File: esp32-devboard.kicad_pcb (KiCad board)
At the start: 4 copper layers, 38 parts, among them J1 USB_C_Receptacle_USB2.0_16P, J2 CA, J3 CB, SW1 BOOT, SW2 RST, SW3 FLIP, SW4 FLOP, U1 ESP32-C6-MINI-1/U, U2 AMS1117-3.3

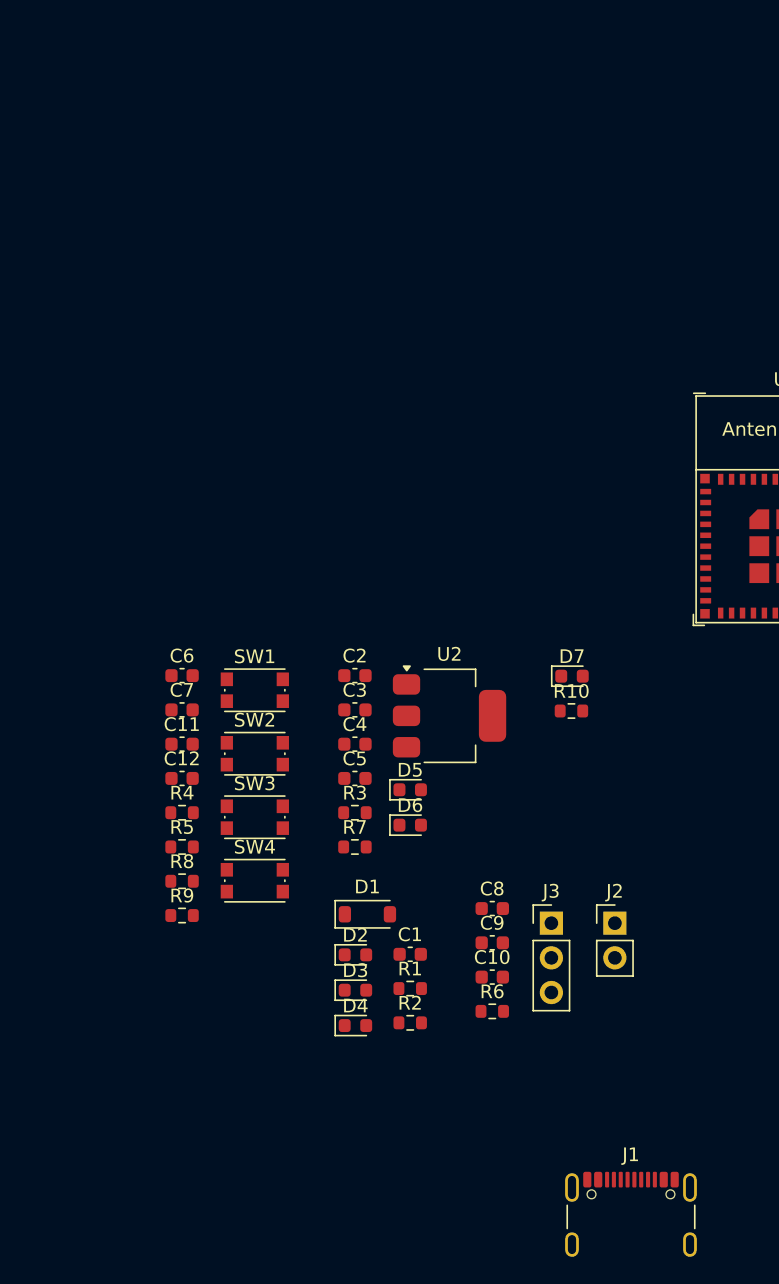
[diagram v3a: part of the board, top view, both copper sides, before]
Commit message: LDO layout>
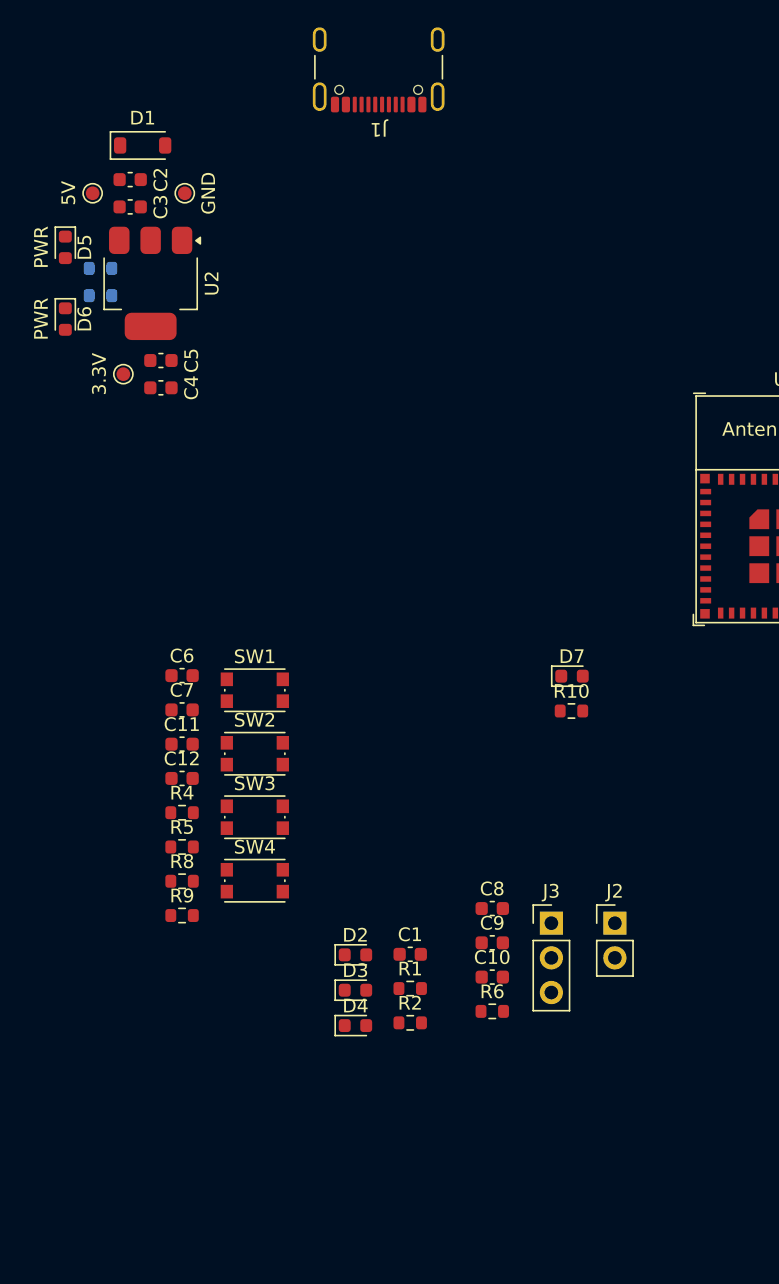
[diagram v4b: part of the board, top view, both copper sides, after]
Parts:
- added TP1: 5V, TestPoint:TestPoint_Pad_D1.0mm, F.Cu at (93.2, 68.0)
- added TP2: 3.3V, TestPoint:TestPoint_Pad_D1.0mm, F.Cu at (95.5, 81.2)
- added TP3: GND, TestPoint:TestPoint_Pad_D1.0mm, F.Cu at (100.0, 68.0)
- R3, R7: moved to B.Cu
- moved J1 88.1 mm to (114.2, 57.8), turned to 180 degrees
- moved D1 58.7 mm to (96.9, 64.5)
- moved D5 47.1 mm to (91.2, 72.0), turned to -90 degrees
- moved D6 44.9 mm to (91.2, 77.2), turned to -90 degrees
- moved R7 44.5 mm to (93.8, 75.5), turned to 180 degrees
- moved R3 44.0 mm to (93.8, 73.5), turned to 180 degrees
- moved C3 40.3 mm to (96.0, 69.0)
- moved C2 39.9 mm to (96.0, 67.0)
- moved U2 38.5 mm to (97.5, 74.6), turned to -90 degrees
- moved C5 33.7 mm to (98.2, 80.2)
- moved C4 29.7 mm to (98.2, 82.2)

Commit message: more pwr stuff
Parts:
- moved TP3 0.25 mm to (100.2, 68.0)
- moved C2 0.22 mm to (96.2, 67.0)
- moved C3 0.22 mm to (96.2, 69.0)
- moved D1 0.08 mm to (97.0, 64.5)
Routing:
- added copper zone on F.Cu, net +3.3V
- added copper zone on F.Cu, net /Power/+5V
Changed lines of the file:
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@@
 	(footprint "TestPoint:TestPoint_Pad_D1.0mm"
 		(layer "F.Cu")
-		(at 100 68 -90)
+		(at 100.25 68 -90)
 		(descr "SMD pad as test Point, diameter 1.0mm")
 		(tags "test point SMD pad")
@@
 	(footprint "Diode_SMD:D_SOD-123"
 		(layer "F.Cu")
-		(at 96.915 64.5)
+		(at 97 64.5)
 		(descr "SOD-123")
 		(tags "SOD-123")
@@
 	(footprint "Capacitor_SMD:C_0603_1608Metric"
 		(layer "F.Cu")
-		(at 96 67)
+		(at 96.225 67)
 		(descr "Capacitor SMD 0603 (1608 Metric), square (rectangular) end terminal, IPC_7351 nominal, (Body size source: IPC-SM-782 page 76, https://www.pcb-3d.com/wordpress/wp-content/uploads/ipc-sm-782a_amendment_1_and_2.pdf), generated with kicad-footprint-generator")
 		(tags "capacitor")
@@
 	(footprint "Capacitor_SMD:C_0603_1608Metric"
 		(layer "F.Cu")
-		(at 96 69)
+		(at 96.225 69)
 		(descr "Capacitor SMD 0603 (1608 Metric), square (rectangular) end terminal, IPC_7351 nominal, (Body size source: IPC-SM-782 page 76, https://www.pcb-3d.com/wordpress/wp-content/uploads/ipc-sm-782a_amendment_1_and_2.pdf), generated with kicad-footprint-generator")
 		(tags "capacitor")
@@
 	)
 	(zone
+		(net 29)
+		(net_name "+3.3V")
+		(layer "F.Cu")
+		(hatch edge 0.5)
+		(priority 1)
+		(connect_pads yes
+			(clearance 0)
+		)
+		(min_thickness 0.25)
+		(filled_areas_thickness no)
+		(fill yes
+			(thermal_gap 0.5)
+			(thermal_bridge_width 0.5)
+		)
+		(polygon
+			(pts
+				(xy 98.25 82.75) (xy 96.75 82.75) (xy 96 82) (xy 94.75 82) (xy 94.75 80.25) (xy 95.5 79.5) (xy 95.5 78.25)
+				(xy 95.5 78.25) (xy 98.25 78.25)
+			)
+		)
+	)
+	(zone
+		(net 38)
+		(net_name "/Power/+5V")
+		(layer "F.Cu")
+		(hatch edge 0.5)
+		(priority 2)
+		(connect_pads yes
+			(clearance 0)
+		)
+		(min_thickness 0.25)
+		(filled_areas_thickness no)
+		(fill yes
+			(thermal_gap 0.5)
+			(thermal_bridge_width 0.5)
+		)
+		(polygon
+			(pts
+				(xy 96.25 72.75) (xy 94.25 72.75) (xy 94.25 70.25) (xy 93.5 69.5) (xy 92.25 69.5) (xy 92.25 66.5)
+				(xy 93.75 66.5) (xy 94.5 65.75) (xy 94.5 63.25) (xy 96.25 63.25)
+			)
+		)
+	)
+	(zone
+		(net 29)
+		(net_name "+3.3V")
+		(layer "F.Cu")
+		(hatch edge 0.5)
+		(connect_pads yes
+			(clearance 0)
+		)
+		(min_thickness 0.25)
+		(filled_areas_thickness no)
+		(fill yes
+			(thermal_gap 0.5)
+			(thermal_bridge_width 0.5)
+		)
+		(polygon
+			(pts
+				(xy 95.5 79) (xy 95.5 76.5) (xy 95.5 76.5) (xy 96.5 75.5) (xy 96.5 70.25) (xy 98.5 70.25) (xy 98.5 75.5)
+				(xy 99.5 76.5) (xy 99.5 76.5) (xy 99.5 79)
+			)
+		)
+	)
+	(zone
 		(net 0)
 		(net_name "")
@@
 		(members "9e491c97-c408-47aa-a825-656574b5255b" "efe0206d-e05d-4263-8e52-4d6ee51e22c0")
 	)
-	(group ""
-		(members "1b6c8068-067f-474c-ba5a-769a4012d6b8" "262f769d-a23a-4fdd-95f2-37f04a277f88"
-			"486c2cc9-136b-4f64-8c2a-f94eec6c1d56" "4a1526ff-0a48-487e-8273-066df841240d"
-			"54078b00-5d86-4ed3-92e5-de67855fb4d0" "5a667fe3-618f-45d0-b3d5-f59ddde55a9a"
-			"7ea36561-44c1-4dda-9039-b84add404954" "9e30236c-4aae-4ac8-98ee-09181bec6437"
-			"a3e8463d-94b6-462c-b727-42dbfcba4cf4" "bd917cb7-f533-4c32-a060-e98790d32795"
-			"d6df7a0d-5dc7-41a9-8d43-eab22e0207d0" "dd98eb8f-062d-48e5-8fa0-3628e489a757"
-		)
-	)
 )

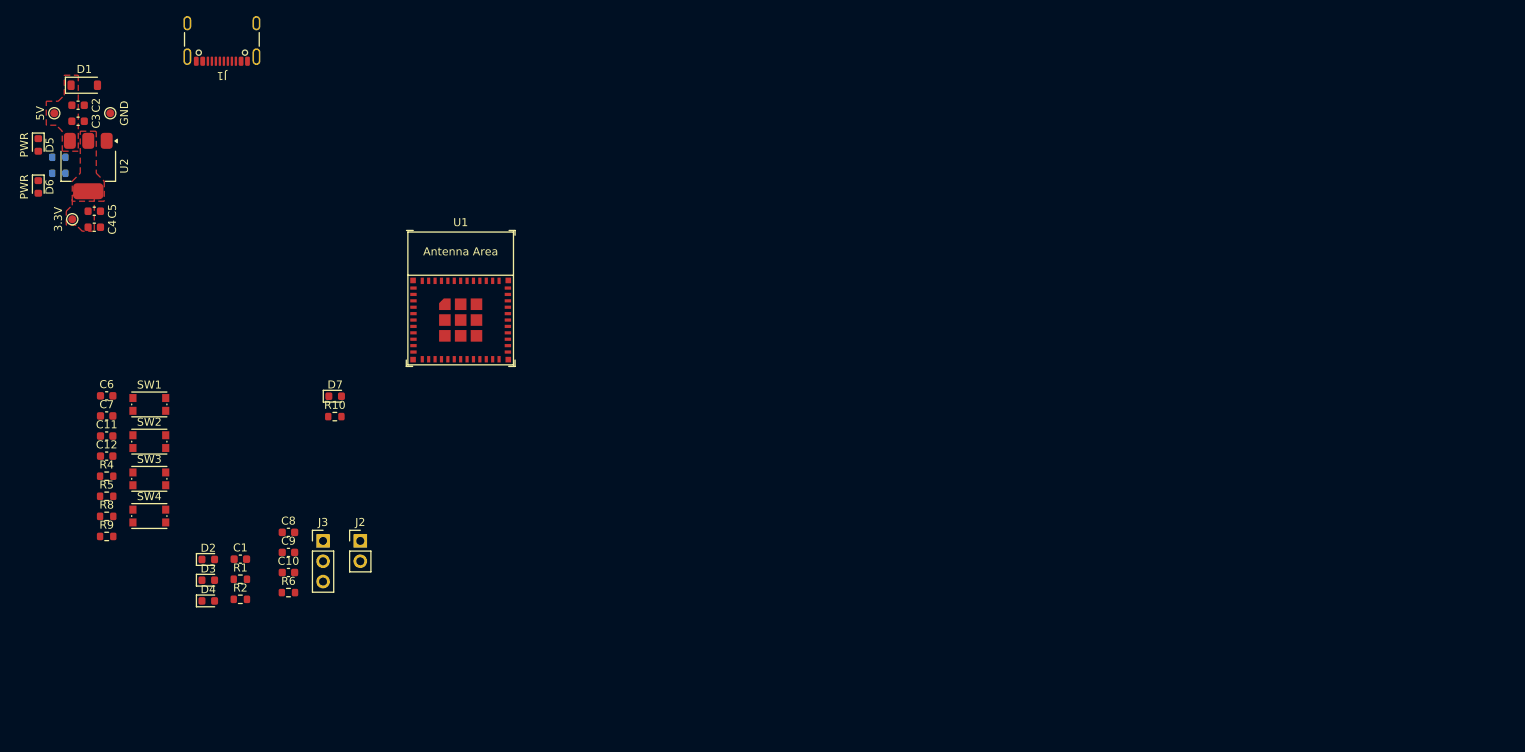
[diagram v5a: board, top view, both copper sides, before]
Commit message: more layout & custom edge cuts
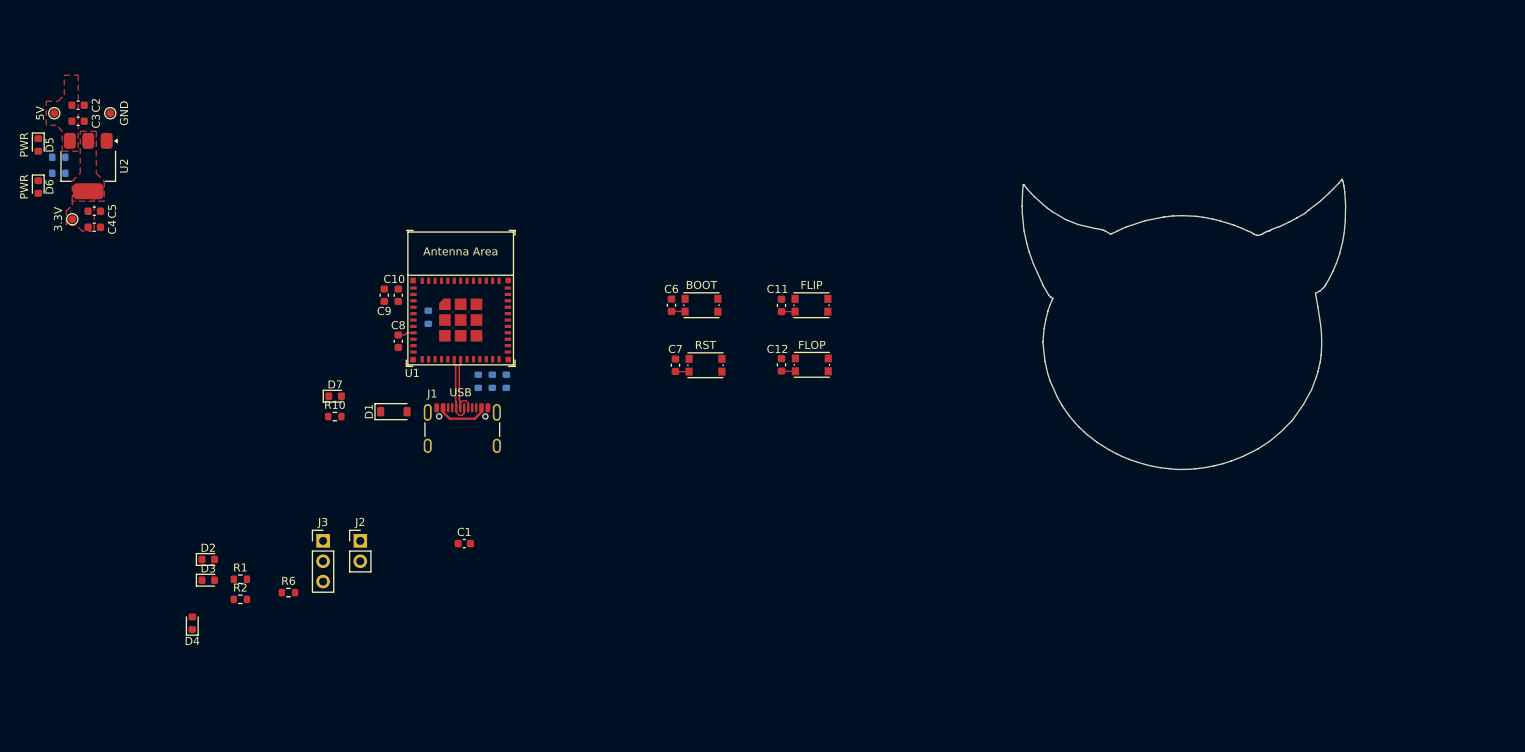
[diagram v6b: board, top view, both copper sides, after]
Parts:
- R4, R5, R8, R9: moved to B.Cu
- moved C11 85.9 mm to (184.2, 92.0), turned to 90 degrees
- moved SW3 85.6 mm to (187.9, 92.0)
- moved C12 85.1 mm to (184.2, 99.5), turned to 90 degrees
- moved SW4 84.9 mm to (187.9, 99.5)
- moved C6 71.5 mm to (170.4, 92.0), turned to 90 degrees
- moved C7 71.4 mm to (170.9, 99.5), turned to 90 degrees
- moved SW2 70.2 mm to (174.7, 99.5)
- moved SW1 70.1 mm to (174.2, 92.0)
- moved J1 58.9 mm to (144.2, 108.5), turned to 0 degrees
- moved D1 56.2 mm to (135.7, 105.3)
- moved R9 52.0 mm to (148.0, 101.5), turned to 90 degrees
- moved R4 51.3 mm to (149.8, 101.5), turned to 90 degrees
- moved R8 49.4 mm to (146.2, 101.5), turned to 90 degrees
- moved R5 46.0 mm to (140.0, 93.5), turned to -90 degrees
- moved C10 37.3 mm to (136.2, 90.8), turned to 90 degrees
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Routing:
- net /ESP32/USB_D-: track 0.00 -> 8.68 mm
- net /ESP32/USB_D+: track 0.00 -> 8.57 mm
- net /USB/VBUSB: track 0.00 -> 6.54 mm
- net /Devices/RST: track 0.00 -> 3.72 mm
- net /Devices/FLOP: track 0.00 -> 1.76 mm
- net /Devices/BOOT: track 0.00 -> 1.71 mm
- net /Devices/FLIP: track 0.00 -> 1.70 mm
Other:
- board outline added: 40.4 x 36.3 mm
- board text added: "USB"

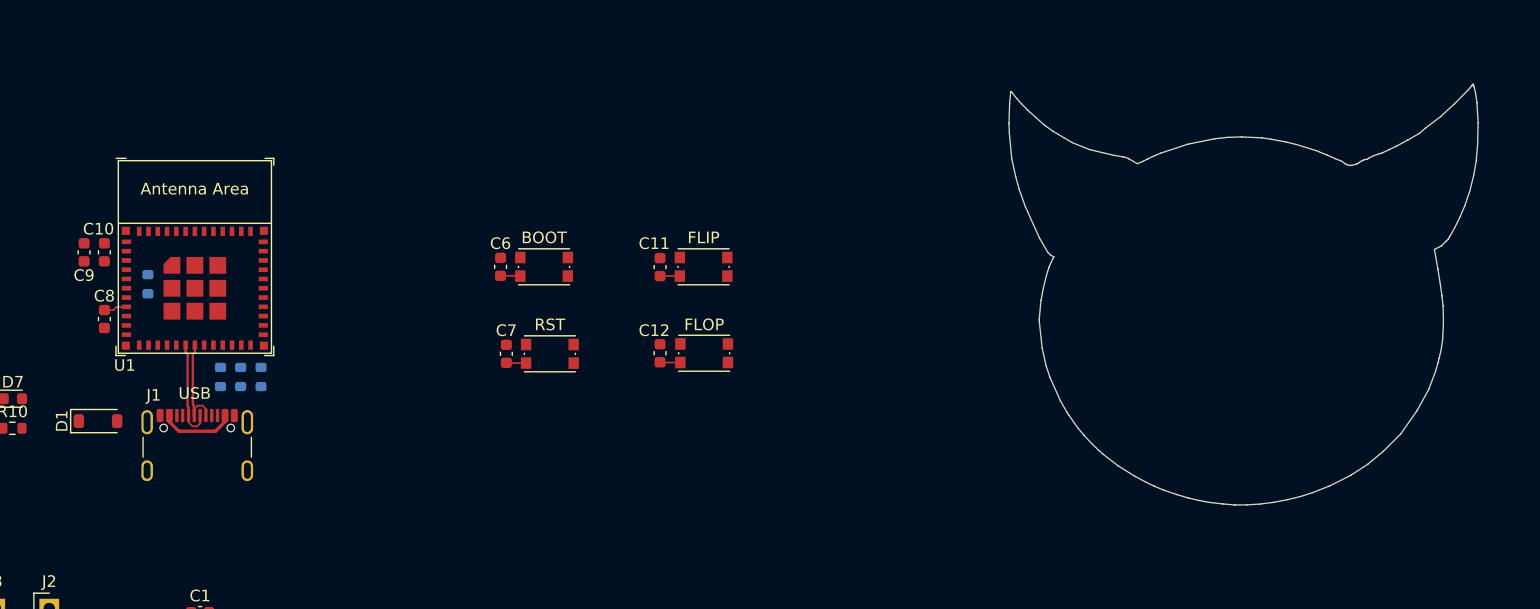
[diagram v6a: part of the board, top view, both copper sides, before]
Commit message: zone fills & button layout
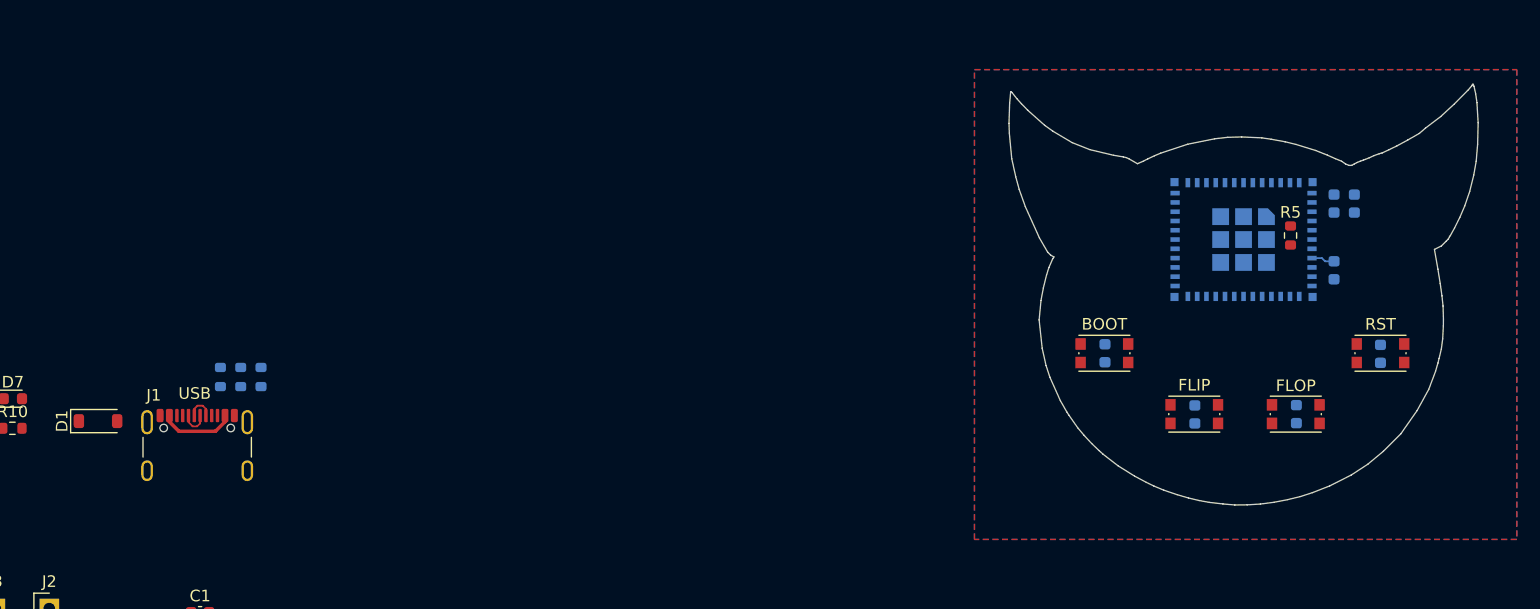
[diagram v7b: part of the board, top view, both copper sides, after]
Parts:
- C10, C11, C12, C6, C7, C8, C9, U1: moved to B.Cu
- R5: moved to F.Cu
- moved C9 109.6 mm to (244.0, 86.5)
- moved C10 106.1 mm to (242.2, 86.5)
- moved C8 106.1 mm to (242.2, 92.3)
- moved R5 98.6 mm to (238.5, 89.3)
- moved U1 90.5 mm to (234.4, 87.0), turned to 180 degrees
- moved C7 75.3 mm to (246.2, 99.5)
- moved SW2 71.6 mm to (246.2, 99.5)
- moved C12 55.1 mm to (239.0, 104.7)
- moved C6 52.6 mm to (222.5, 99.5)
- moved SW4 51.3 mm to (238.9, 104.7)
- moved SW1 48.9 mm to (222.4, 99.5)
- moved C11 47.8 mm to (230.2, 104.7)
- moved SW3 44.2 mm to (230.2, 104.7)
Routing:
- net /ESP32/USB_D+: track 8.57 -> 2.38 mm
- net /ESP32/USB_D-: track 8.68 -> 2.51 mm
- net /Devices/FLOP: track 1.76 -> 0.00 mm
- net /Devices/BOOT: track 1.71 -> 0.00 mm
- net /Devices/RST: track 3.72 -> 2.01 mm
- net /Devices/FLIP: track 1.70 -> 0.00 mm
- added copper zone on In2.Cu, net +3.3V
- added copper zone on B.Cu, net GND
- added copper zone on In1.Cu, net GND
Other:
- outline, holes or cut-outs redrawn

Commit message: more layout (dont look at this)
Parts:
- D1, J1, R5, U2: moved to B.Cu
- moved C2 173.7 mm to (268.2, 91.0)
- moved C3 173.7 mm to (268.2, 93.0)
- moved C4 173.7 mm to (270.2, 106.2)
- moved C5 173.7 mm to (270.2, 104.2)
- moved R3 173.7 mm to (265.8, 97.5)
- moved R7 173.7 mm to (265.8, 99.5)
- moved TP1 173.7 mm to (265.2, 92.0)
- moved TP2 173.7 mm to (267.5, 105.2)
- moved TP3 173.7 mm to (272.2, 92.0)
- moved U2 148.8 mm to (243.8, 102.2), turned to 90 degrees
- moved D6 146.7 mm to (237.5, 89.2), turned to 90 degrees
- moved D5 141.1 mm to (231.2, 89.2), turned to 90 degrees
- moved D1 105.6 mm to (241.2, 109.3), turned to -90 degrees
- moved J1 90.2 mm to (234.4, 109.0), turned to 180 degrees
- moved R5 5.65 mm to (244.0, 90.6)
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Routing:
- added copper zone on B.Cu, net +3.3V
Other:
- outline, holes or cut-outs redrawn
